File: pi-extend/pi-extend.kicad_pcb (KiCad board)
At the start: 2 copper layers, 58.4 x 67.1 mm, 5 parts, among them J1 Conn_02x20_Odd_Even, J2 Conn_01x20_Male, J3 Conn_01x20_Male, J4 Conn_01x02_Male, J5 Conn_01x02_Male

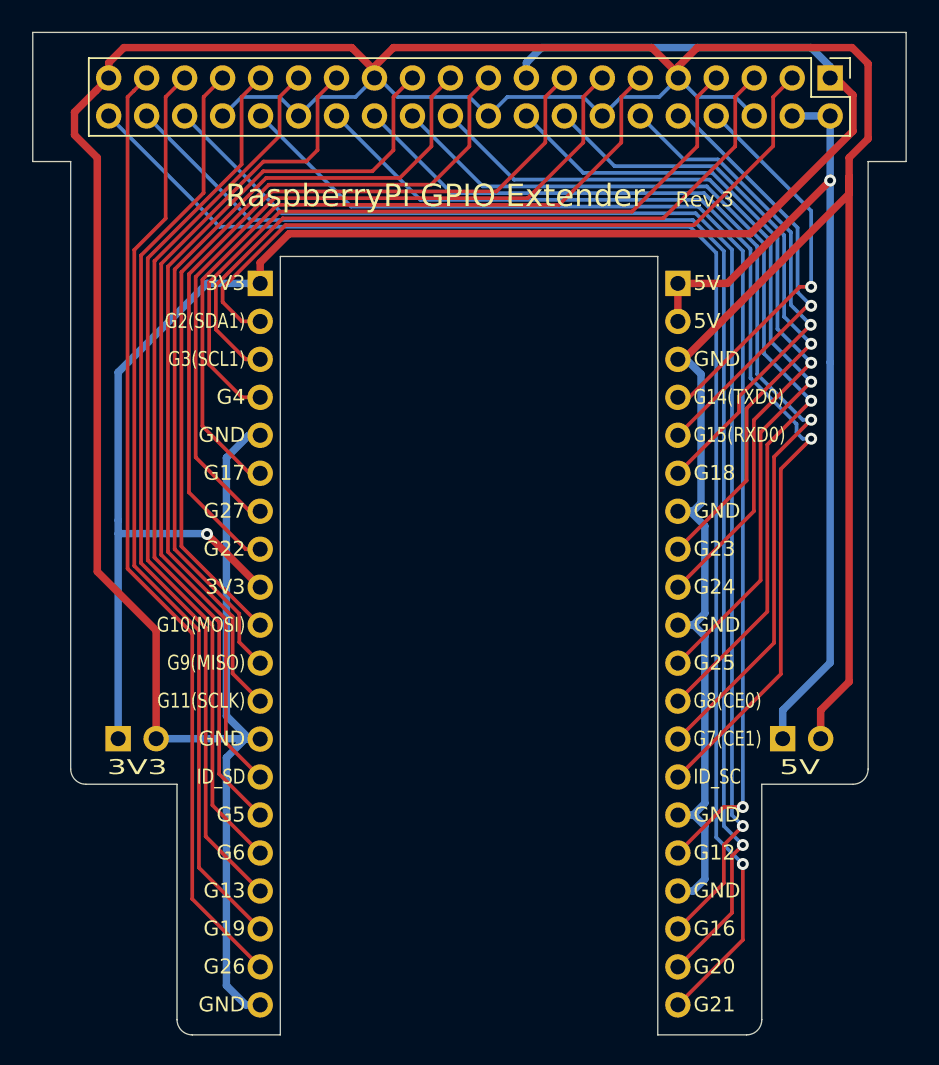
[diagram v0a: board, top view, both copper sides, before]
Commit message: [pi-extend] 크기 야간 줄임
Signed-off-by: Ju, Gyeong-min <jcmh74@gmail.com>
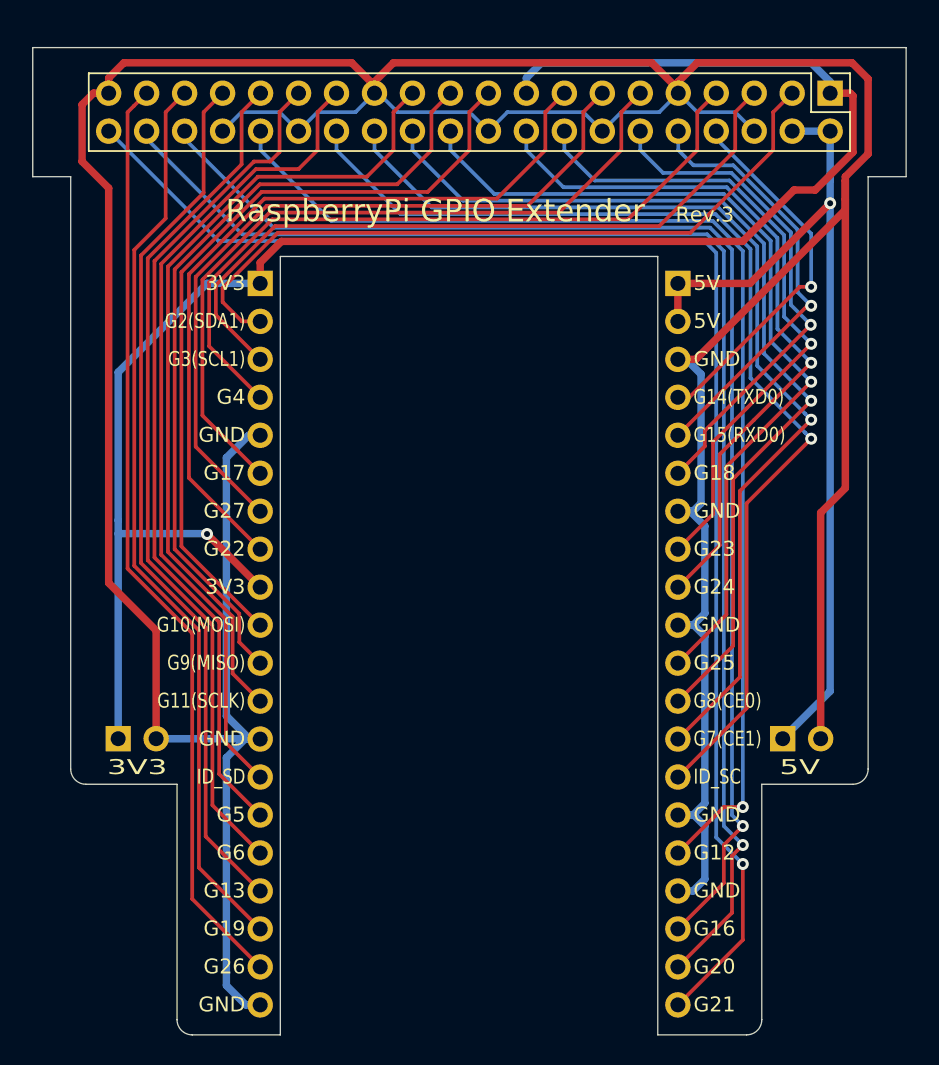
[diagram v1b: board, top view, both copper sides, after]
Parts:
- moved J1 1.02 mm to (186.9, 66.0)
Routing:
- net GND: track 306.9 -> 305.2 mm
- net +5V: track 61.1 -> 59.4 mm
- net Net-(J1-Pad7): track 51.3 -> 49.8 mm
- net Net-(J1-Pad5): track 50.4 -> 49.0 mm
- net Net-(J1-Pad15): track 53.3 -> 52.0 mm
- net Net-(J1-Pad13): track 52.4 -> 51.2 mm
- net Net-(J1-Pad11): track 51.6 -> 50.5 mm
- net Net-(J1-Pad8): track 26.0 -> 25.0 mm
- net Net-(J1-Pad35): track 61.8 -> 60.8 mm
- net Net-(J1-Pad33): track 59.9 -> 58.9 mm
- net Net-(J1-Pad23): track 55.3 -> 54.3 mm
- net Net-(J1-Pad31): track 58.1 -> 57.1 mm
- net Net-(J1-Pad27): track 56.0 -> 55.0 mm
- net Net-(J1-Pad37): track 63.7 -> 62.6 mm
- net Net-(J1-Pad21): track 54.4 -> 53.5 mm
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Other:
- board size 58.4 x 67.1 mm -> 58.4 x 66 mm

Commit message: pi-extend 배선 조정
Signed-off-by: Ju, Gyeong-min <jcmh74@gmail.com>
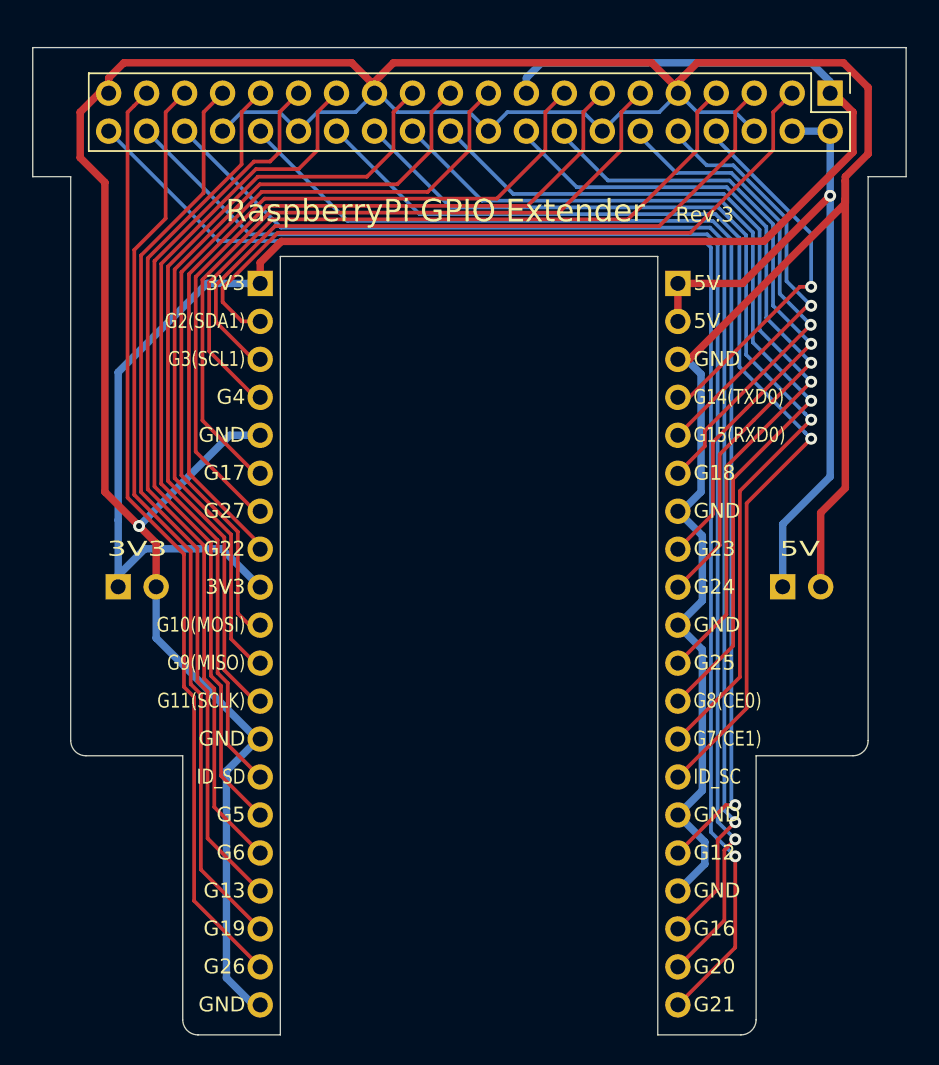
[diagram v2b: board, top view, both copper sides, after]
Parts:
- moved J4 10.2 mm to (139.3, 99.1)
- moved J5 10.2 mm to (183.8, 99.1)
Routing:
- net GND: track 305.2 -> 272.9 mm, vias 0 -> 1
- net +5V: track 59.4 -> 49.5 mm
- net +3V3: track 120.0 -> 110.3 mm, vias 1 -> 0
- net Net-(J1-Pad32): track 79.1 -> 77.7 mm
- net Net-(J1-Pad28): track 72.4 -> 71.6 mm
- net Net-(J1-Pad26): track 67.7 -> 66.9 mm
- net Net-(J1-Pad22): track 58.3 -> 57.5 mm
- net Net-(J1-Pad24): track 63.0 -> 62.2 mm
- net Net-(J1-Pad38): track 92.4 -> 91.7 mm
- net Net-(J1-Pad36): track 87.7 -> 87.0 mm
- net Net-(J1-Pad12): track 34.0 -> 33.4 mm
- net Net-(J1-Pad10): track 29.9 -> 29.4 mm
- net Net-(J1-Pad18): track 48.5 -> 48.0 mm
- net Net-(J1-Pad16): track 43.8 -> 43.3 mm
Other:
- outline, holes or cut-outs redrawn

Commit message: pi-extend 전원핀 배치 변경
Signed-off-by: Ju, Gyeong-min <jcmh74@gmail.com>
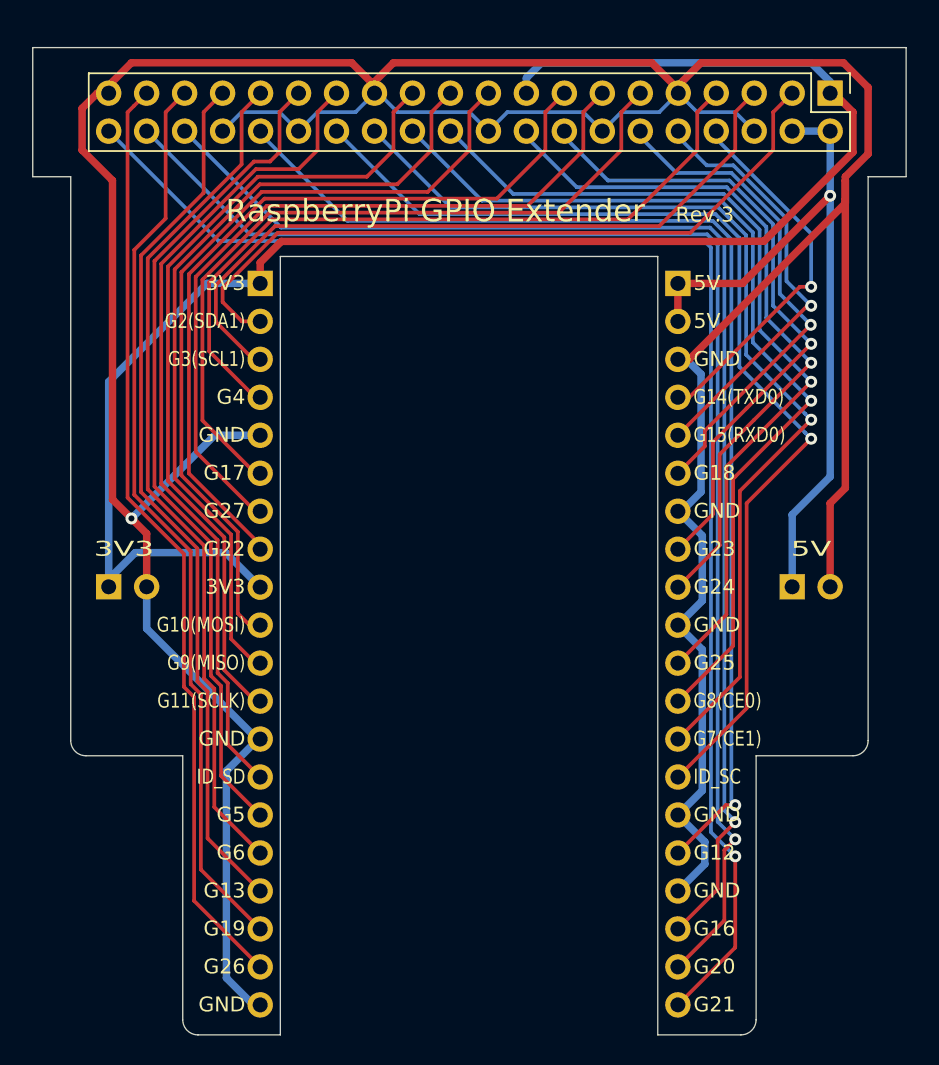
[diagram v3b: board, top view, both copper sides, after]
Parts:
- moved J4 0.63 mm to (138.7, 99.1)
- moved J5 0.63 mm to (184.4, 99.1)
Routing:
- net +3V3: track 110.3 -> 110.8 mm

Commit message: pi-extend 커넥터 부품 변경
Signed-off-by: Ju, Gyeong-min <jcmh74@gmail.com>
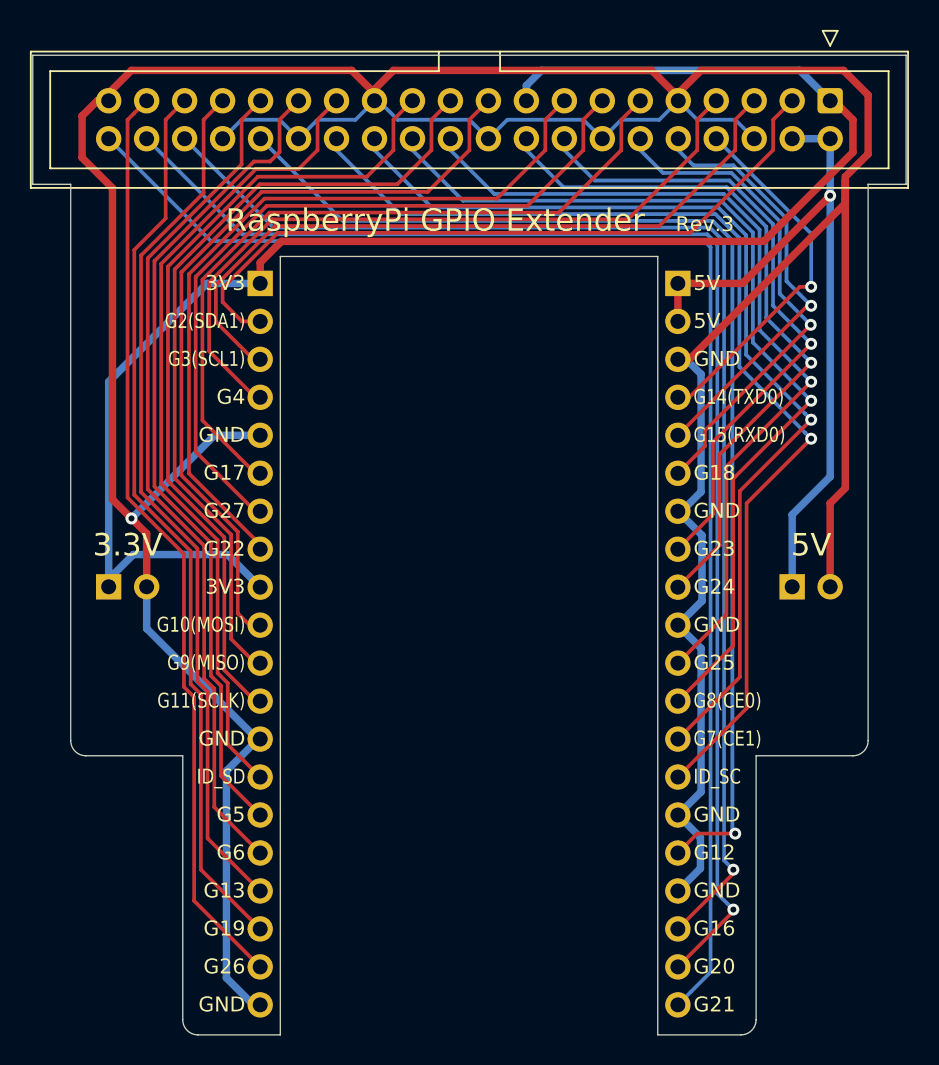
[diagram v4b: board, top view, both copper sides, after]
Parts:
- J1: footprint Connector_PinHeader_2.54mm:PinHeader_2x20_P2.54mm_Vertical -> Connector_IDC:IDC-Header_2x20_P2.54mm_Vertical
- moved J1 0.51 mm to (186.9, 66.5)
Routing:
- net Net-(J1-Pad40): track 96.4 -> 94.9 mm, vias 1 -> 0
- net GND: track 272.4 -> 271.1 mm
- net +3V3: track 110.8 -> 109.7 mm
- net Net-(J1-Pad32): track 77.7 -> 78.7 mm
- net Net-(J1-Pad29): track 55.8 -> 55.3 mm
- net Net-(J1-Pad5): track 49.3 -> 48.8 mm
- net Net-(J1-Pad35): track 60.8 -> 60.3 mm
- net Net-(J1-Pad31): track 57.1 -> 56.6 mm
- net Net-(J1-Pad15): track 52.0 -> 51.5 mm
- net Net-(J1-Pad13): track 51.4 -> 50.9 mm
- net Net-(J1-Pad7): track 49.9 -> 49.4 mm
- net Net-(J1-Pad33): track 58.9 -> 58.4 mm
- net Net-(J1-Pad3): track 49.0 -> 48.5 mm
- net Net-(J1-Pad27): track 55.0 -> 54.5 mm
- net Net-(J1-Pad23): track 54.5 -> 54.0 mm
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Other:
- board size 58.4 x 66 mm -> 58.4 x 65.5 mm
- board text added: "3.3V"

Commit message: pi-extend 보드 마킹 추가
Signed-off-by: Ju, Gyeong-min <jcmh74@gmail.com>
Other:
- board text added: "GND 3V3"
- board text added: "GND 5V"

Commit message: pi-extend rev4 업그레이드
Signed-off-by: Ju, Gyeong-min <jcmh74@gmail.com>
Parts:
- added J6: Conn_01x02_Male, Connector_PinHeader_2.54mm:PinHeader_1x02_P2.54mm_Vertical, B.Cu at (138.7, 104.1)
- added J7: Conn_01x02_Male, Connector_PinHeader_2.54mm:PinHeader_1x02_P2.54mm_Vertical, B.Cu at (184.4, 104.1)
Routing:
- net +3V3: track 109.7 -> 117.5 mm
- net GND: track 271.1 -> 278.3 mm
- net +5V: track 49.2 -> 53.9 mm, vias 1 -> 0
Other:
- board text added: "<1"
- board text added: "Rev.4"
- board text removed: "Rev.3"
